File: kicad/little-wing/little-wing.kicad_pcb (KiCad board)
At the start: 4 copper layers, 14 x 42.1 mm, 68 parts, among them J1 HRO_TYPE-C-31-M-14, J2 Battery, J3 rgb, J4 columns, J5 Conn_01x10, J6 rows, J7 sensor, Q1 AO3401A, Q2 2N7002, SW1 Battery, SW2 Reset, U1 nRF52840_CKAA, U2 nPM1100-CAAx, X1 32MHz, X2 32.768kHz

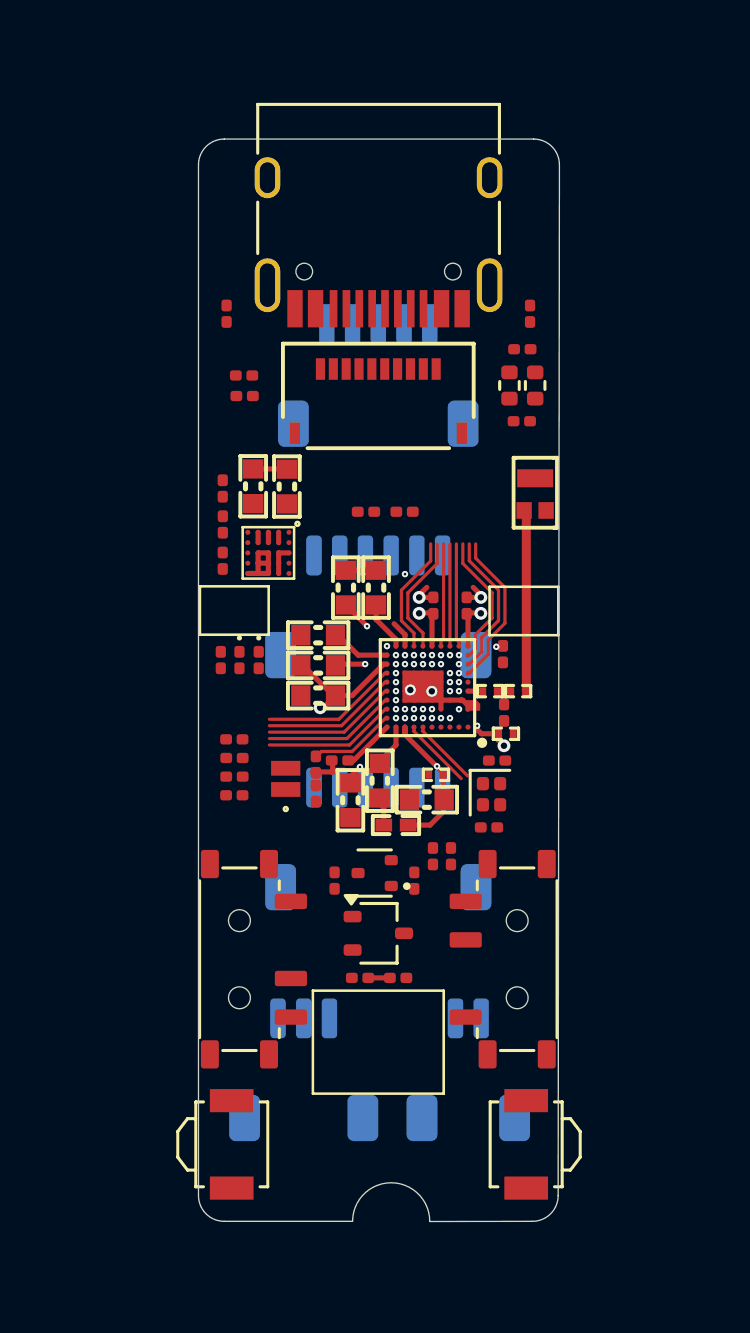
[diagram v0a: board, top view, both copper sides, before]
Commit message: Loosely attaching pins to prefiery
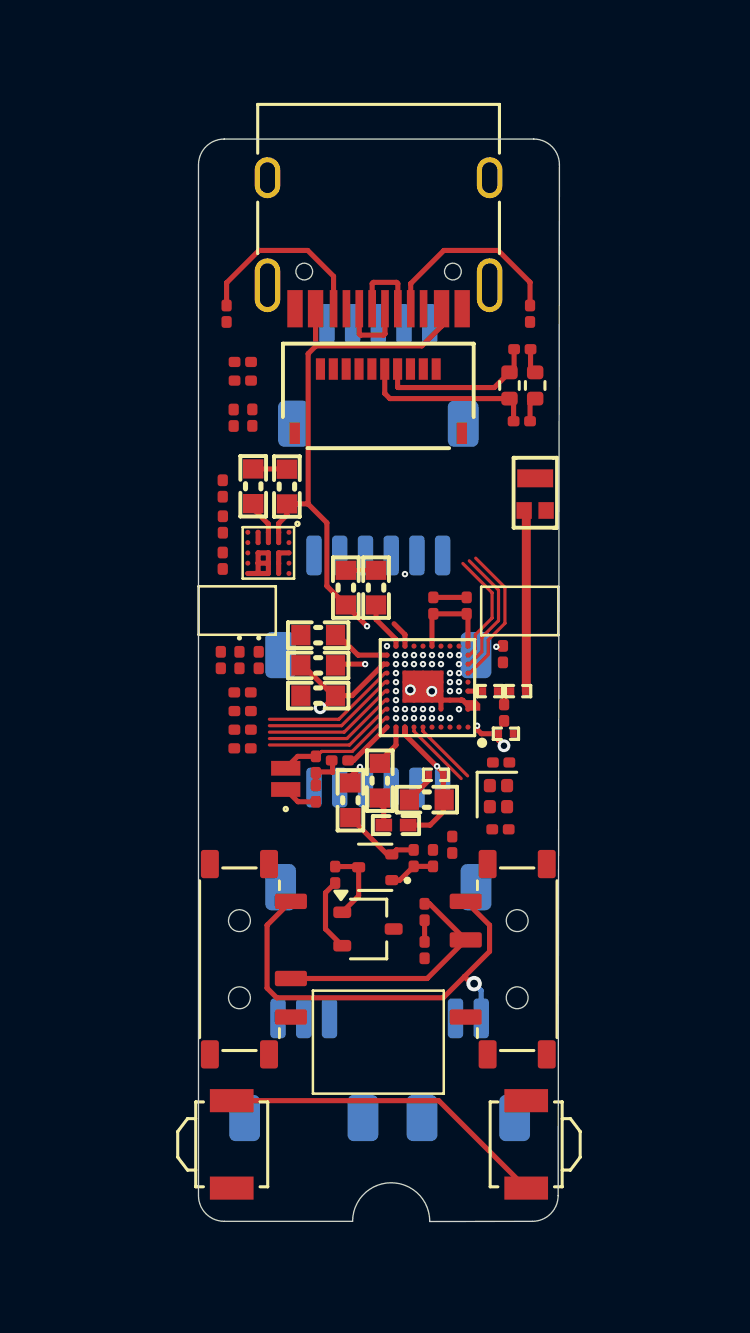
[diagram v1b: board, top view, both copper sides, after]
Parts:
- moved R32 6.96 mm to (145.1, 68.4), turned to -90 degrees
- moved R33 6.31 mm to (144.4, 68.4), turned to -90 degrees
- moved R_DIV1 3.59 mm to (151.8, 87.7), turned to -90 degrees
- moved R11 1.85 mm to (144.7, 79.1)
- moved R14 1.85 mm to (144.7, 79.8)
- moved R15 1.85 mm to (144.7, 80.6)
- moved R16 1.85 mm to (144.7, 81.3)
- moved R_DIV2 1.49 mm to (151.8, 89.1), turned to -90 degrees
- moved R18 0.88 mm to (151.4, 85.6)
- moved R39 0.60 mm to (144.7, 67.0)
- moved C37 0.53 mm to (144.7, 66.3)
- moved C2 0.45 mm to (154.8, 84.5)
- moved R8 0.45 mm to (152.9, 85.0)
- moved Q1 0.44 mm to (149.6, 88.3)
- moved X1 0.28 mm to (154.7, 83.2)
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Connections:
- J7 pad 1: GND -> VDD
- J7 pad 6: VDD -> GND
- U1 pad A5: unconnected-(U1-P0.03/AIN1-PadA5) -> VSENSE
- U1 pad A6: unconnected-(U1-P0.28/AIN4-PadA6) -> RGB DATA
- U1 pad A7: unconnected-(U1-P0.30/AIN6-PadA7) -> RGB ON
- U1 pad C10: unconnected-(U1-P0.04/AIN2-PadC10) -> Sensor IRQ
- U1 pad C8: VSENSE -> unconnected-(U1-P0.31/AIN7-PadC8)
- U1 pad D10: unconnected-(U1-P0.05/AIN3-PadD10) -> Sensor CLK
- U1 pad E10: unconnected-(U1-P0.08-PadE10) -> Sensor SDIO
- U1 pad F10: unconnected-(U1-P1.09-PadF10) -> Sensor CS
- U1 pad G1: unconnected-(U1-P1.07-PadG1) -> LCD CS
- U1 pad H1: unconnected-(U1-P1.04-PadH1) -> LCD DATA
- U1 pad J1: unconnected-(U1-P1.01-PadJ1) -> LCD CLK
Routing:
- net VBUS: track 3.49 -> 25.1 mm
- net Net-(J2-Pin_1): track 0.00 -> 17.6 mm, vias 0 -> 1
- net VBAT: track 0.70 -> 10.3 mm
- net RST: track 4.69 -> 12.9 mm
- net Net-(J1-CC1): track 0.00 -> 7.57 mm
- net Net-(J1-CC2): track 0.00 -> 7.24 mm
- net unconnected-(U1-P0.31/AIN7-PadC8): track 0.00 -> 7.05 mm, vias 0 -> 2
- net VSENSE: track 7.89 -> 0.84 mm, vias 2 -> 0
- net VDDA: track 0.00 -> 6.83 mm
- net VDD: track 15.4 -> 21.8 mm, vias 8 -> 6
- net unconnected-(U1-P1.07-PadG1): track 6.13 -> 0.00 mm
- net unconnected-(U1-P1.04-PadH1): track 5.67 -> 0.00 mm
- net LCD CS: track 0.00 -> 5.57 mm
- net unconnected-(U1-P1.09-PadF10): track 5.27 -> 0.00 mm
- net Sensor CS: track 0.00 -> 5.27 mm
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
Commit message: More routing
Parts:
- moved R11 0.12 mm to (144.8, 79.1)
- moved R15 0.12 mm to (144.8, 80.5)
- moved R16 0.12 mm to (144.8, 81.3)
- moved R14 0.12 mm to (144.8, 79.8)
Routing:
- net Net-(J3-Pin_2): track 0.00 -> 10.3 mm, vias 0 -> 1
- net Net-(J7-Pin_2): track 0.00 -> 9.98 mm, vias 0 -> 1
- net VSENSE: track 0.84 -> 10.7 mm
- net LCD CLK: track 4.46 -> 14.2 mm
- net LCD DATA: track 5.02 -> 14.6 mm
- net LCD CS: track 5.57 -> 15.0 mm
- net Net-(J7-Pin_3): track 0.00 -> 8.70 mm, vias 0 -> 1
- net Net-(J7-Pin_4): track 0.00 -> 7.38 mm, vias 0 -> 1
- net Net-(J7-Pin_5): track 0.00 -> 6.05 mm, vias 0 -> 1
- net unconnected-(U1-P1.05-PadG2): track 5.88 -> 0.00 mm
- net unconnected-(U1-P0.07-PadF9): track 5.75 -> 0.00 mm
- net unconnected-(U1-P0.06-PadE9): track 5.71 -> 0.00 mm
- net unconnected-(U1-P1.08-PadG9): track 5.79 -> 0.11 mm
- net unconnected-(U1-P0.27-PadD9): track 5.67 -> 0.00 mm
- net unconnected-(U1-P0.26-PadC9): track 5.63 -> 0.00 mm
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
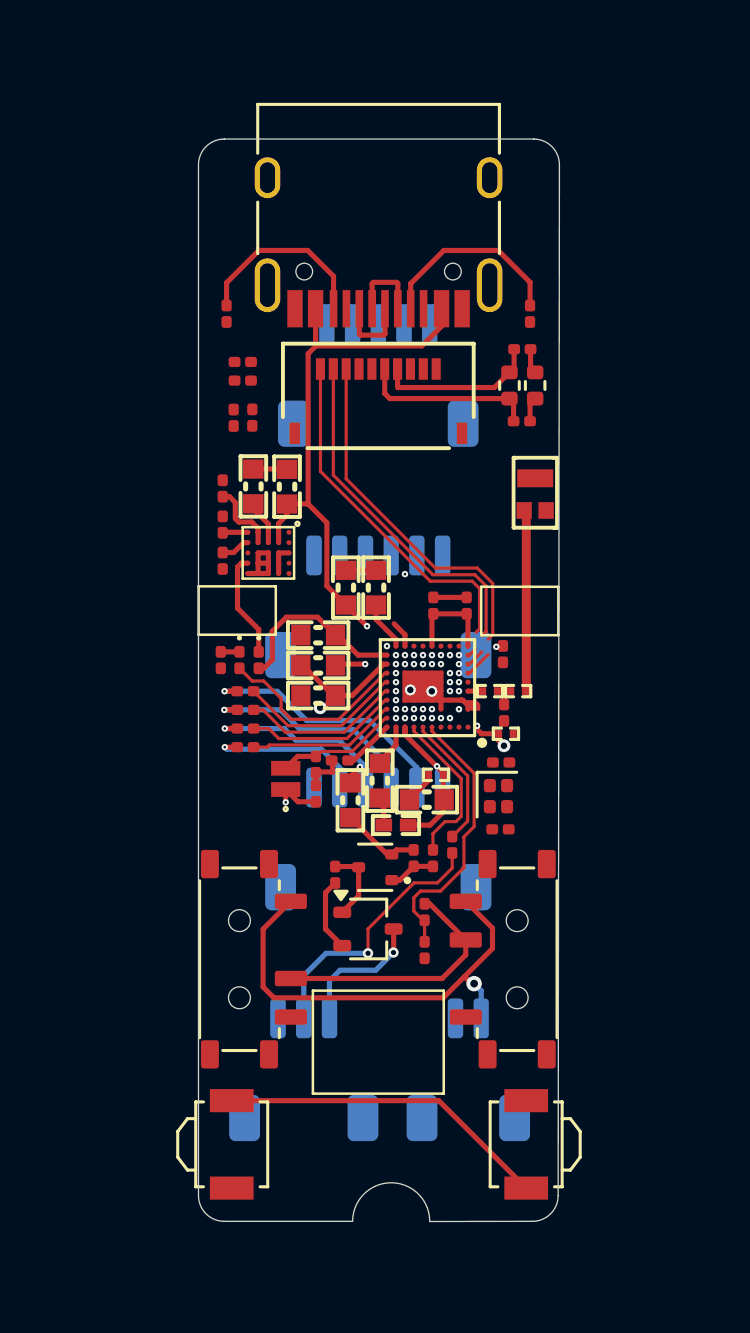
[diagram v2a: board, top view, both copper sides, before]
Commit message: Connecting most of the other components
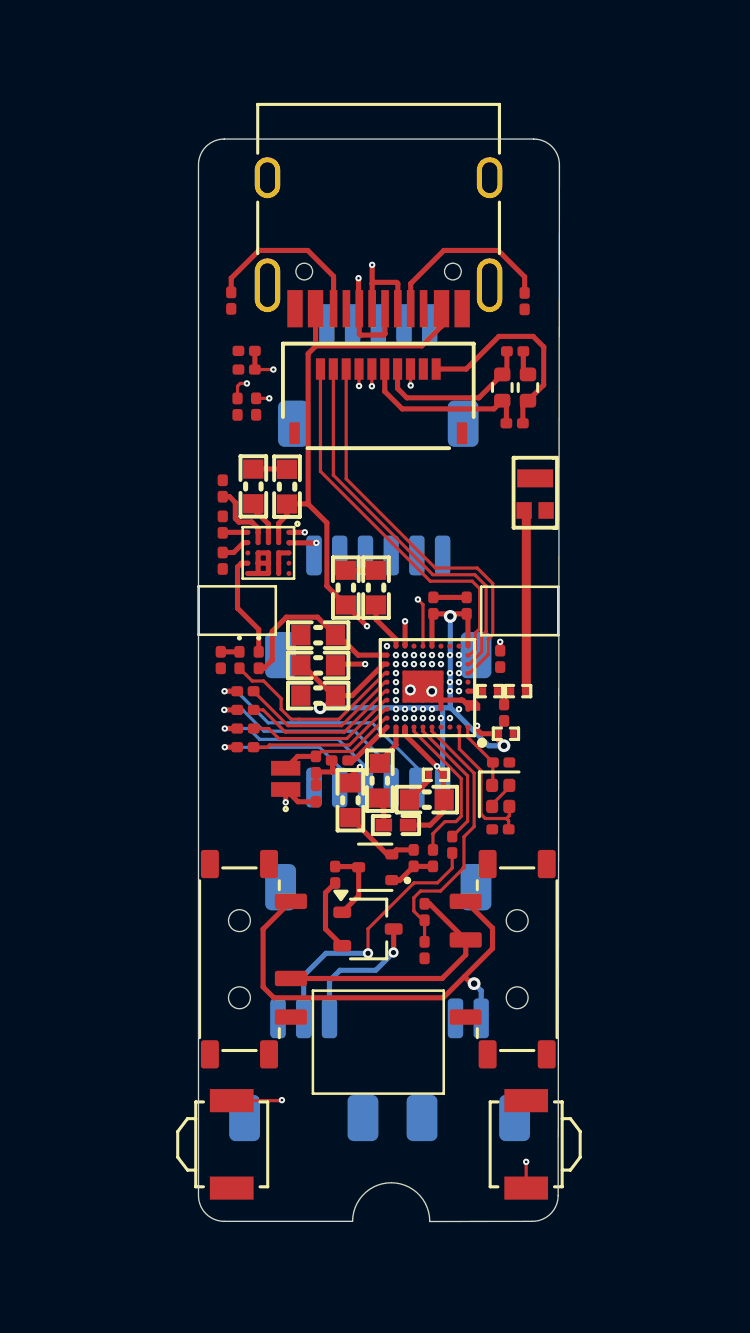
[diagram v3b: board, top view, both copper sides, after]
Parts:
- moved R22 0.54 mm to (144.3, 63.9)
- moved R21 0.53 mm to (155.7, 63.9)
- moved C37 0.46 mm to (144.9, 65.8)
- moved R39 0.46 mm to (144.9, 66.6)
- moved R32 0.46 mm to (145.2, 68.0)
- moved R33 0.46 mm to (144.5, 68.0)
- moved C30 0.29 mm to (155.3, 68.7)
- moved C38 0.29 mm to (155.3, 65.9)
- moved FB1 0.29 mm to (154.8, 67.3)
- moved FB2 0.29 mm to (155.8, 67.3)
- moved C9 0.21 mm to (154.7, 77.8)
- moved X1 0.09 mm to (154.8, 83.2)
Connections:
- X1 pad 2: unconnected-(X1-GND-Pad2) -> GND
- X1 pad 4: unconnected-(X1-GND-Pad4) -> GND
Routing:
- net RST: track 12.9 -> 37.5 mm, vias 0 -> 3
- net D+: track 4.04 -> 26.0 mm, vias 0 -> 3
- net D-: track 6.14 -> 26.1 mm, vias 2 -> 3
- net VDD: track 21.8 -> 37.3 mm, vias 6 -> 7
- net GNDA: track 0.96 -> 8.18 mm
- net EXTMODE: track 0.00 -> 6.86 mm, vias 0 -> 2
- net Net-(J5-Pin_5): track 0.00 -> 6.23 mm, vias 0 -> 2
- net EXTCOMIN: track 0.00 -> 5.95 mm, vias 0 -> 2
- net Net-(U1-XC2): track 0.00 -> 5.77 mm
- net unconnected-(U1-P1.10-PadB4): track 5.38 -> 0.00 mm
- net unconnected-(U1-P1.14-PadB5): track 5.34 -> 0.00 mm
- net unconnected-(U1-P0.02/AIN0-PadB6): track 5.30 -> 0.00 mm
- net Net-(U1-XC1): track 0.00 -> 2.69 mm
- net GND: track 19.5 -> 20.6 mm
- net LCD CLK: track 14.2 -> 14.9 mm
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
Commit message: Connecting remaining power lines
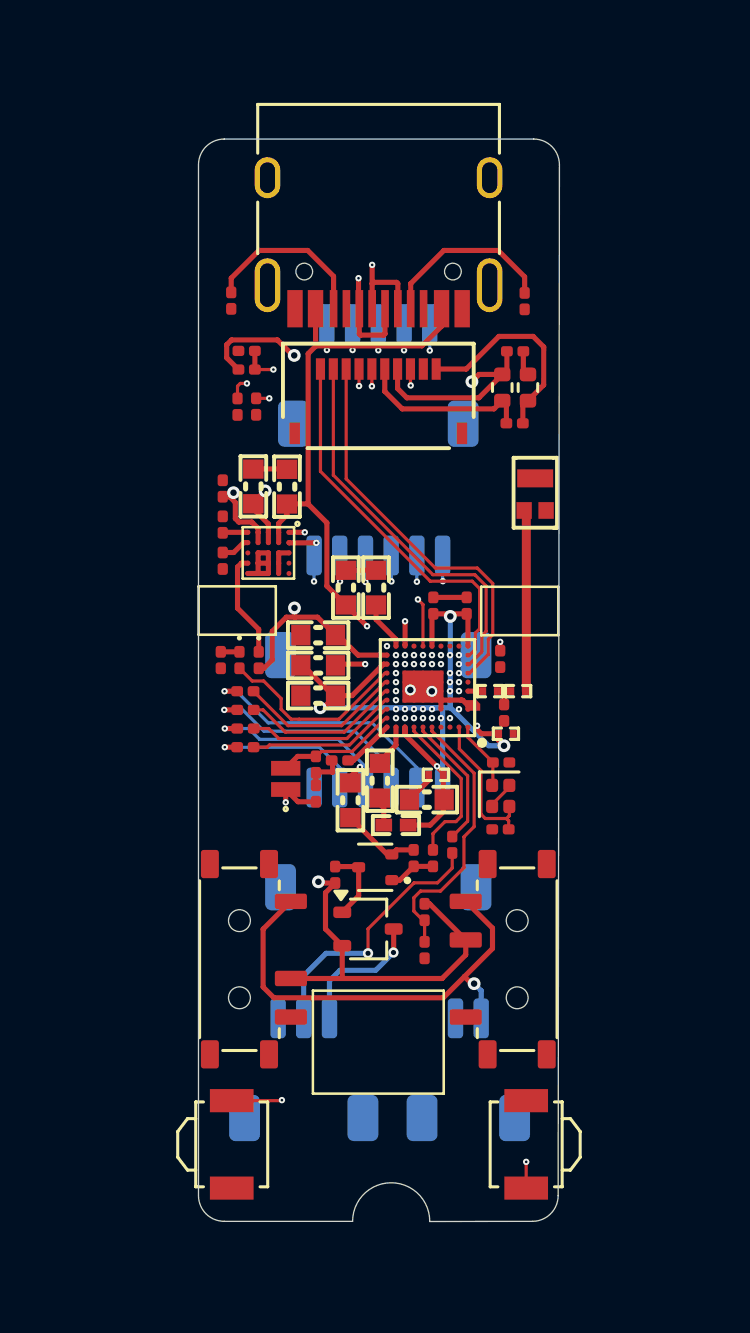
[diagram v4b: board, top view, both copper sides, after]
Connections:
- Q1 pad 2: VSYS -> VBAT
- R10 pad 1: VSYS -> VBAT
- U1 pad C6: unconnected-(U1-P1.15-PadC6) -> Col 5
- U1 pad C7: unconnected-(U1-P0.29/AIN5-PadC7) -> Row 4
- U1 pad C8: unconnected-(U1-P0.31/AIN7-PadC8) -> Col 4
- U1 pad E3: unconnected-(U1-P1.06-PadE3) -> Col 1
- U1 pad F3: unconnected-(U1-P1.03-PadF3) -> Col 0
- U1 pad G3: unconnected-(U1-P1.02-PadG3) -> Col 2
- U1 pad H4: unconnected-(U1-P0.24-PadH4) -> Row 0
- U1 pad H5: unconnected-(U1-P0.23-PadH5) -> Row 1
- U1 pad H6: unconnected-(U1-P0.16-PadH6) -> Col 3
- U1 pad H7: unconnected-(U1-P0.13-PadH7) -> Row 3
- U1 pad H8: unconnected-(U1-P0.11-PadH8) -> Row 2
- X1 pad 2: GND -> unconnected-(X1-GND-Pad2)
- X1 pad 4: GND -> unconnected-(X1-GND-Pad4)
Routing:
- net VDD: track 37.3 -> 59.5 mm, vias 7 -> 9
- net VBAT: track 13.0 -> 34.4 mm, vias 0 -> 2
- net Row 4: track 0.00 -> 17.3 mm, vias 0 -> 3
- net Row 3: track 0.00 -> 15.8 mm, vias 0 -> 3
- net Row 1: track 0.00 -> 15.3 mm, vias 0 -> 3
- net Row 0: track 0.00 -> 15.3 mm, vias 0 -> 3
- net Row 2: track 0.00 -> 14.7 mm, vias 0 -> 3
- net unconnected-(U1-P1.03-PadF3): track 13.4 -> 0.00 mm, vias 2 -> 0
- net unconnected-(U1-P1.06-PadE3): track 12.6 -> 0.00 mm, vias 2 -> 0
- net unconnected-(U1-P1.02-PadG3): track 11.0 -> 0.00 mm, vias 2 -> 0
- net Col 0: track 0.00 -> 10.2 mm, vias 0 -> 3
- net Col 5: track 0.00 -> 9.94 mm, vias 0 -> 3
- net unconnected-(U1-P0.24-PadH4): track 9.56 -> 0.00 mm, vias 2 -> 0
- net unconnected-(U1-P0.23-PadH5): track 9.47 -> 0.00 mm, vias 2 -> 0
- net unconnected-(U1-P0.16-PadH6): track 8.49 -> 0.00 mm, vias 2 -> 0
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
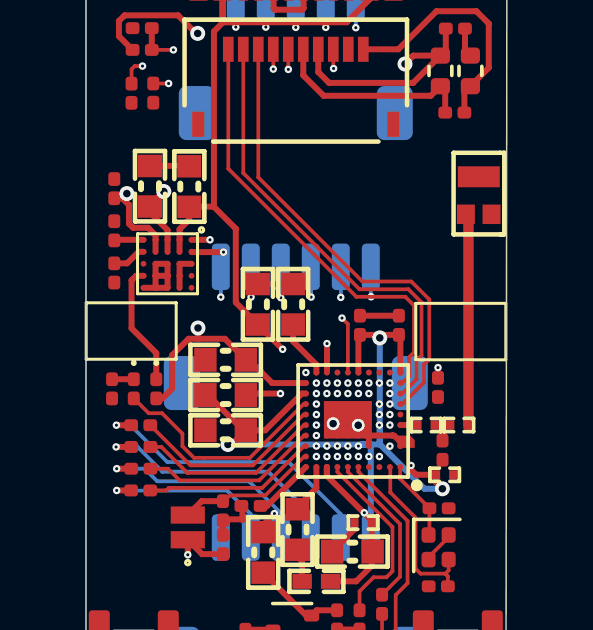
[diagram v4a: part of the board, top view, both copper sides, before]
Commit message: Adding the J-tag connector for the programmer
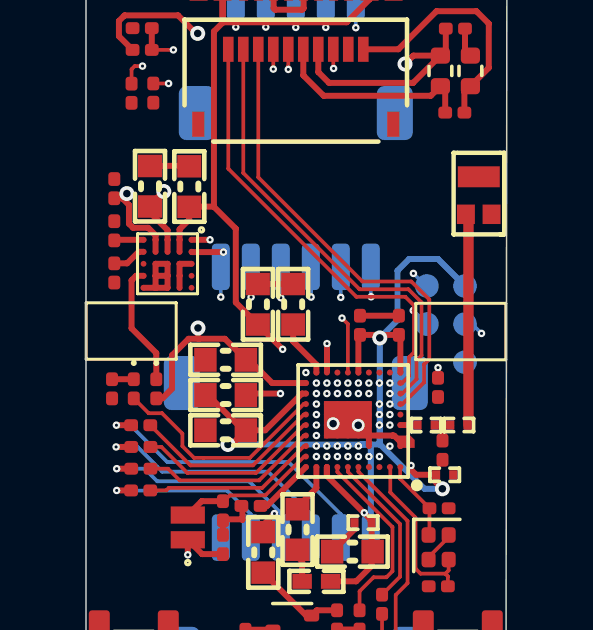
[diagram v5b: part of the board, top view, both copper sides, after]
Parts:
- added J8: Conn_ARM_SWD_TagConnect_TC2030-NL, Connector:Tag-Connect_TC2030-IDC-NL_2x03_P1.27mm_Vertical, B.Cu at (155.0, 75.7)
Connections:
- U1 pad H2: unconnected-(U1-SWDCLK-PadH2) -> SWCLK
- U1 pad J2: unconnected-(U1-SWDIO-PadJ2) -> SWDIO
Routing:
- net VDD: track 59.5 -> 64.8 mm
- net unconnected-(U1-SWDCLK-PadH2): track 4.89 -> 0.00 mm, vias 1 -> 0
- net SWDIO: track 0.00 -> 4.60 mm, vias 0 -> 2
- net unconnected-(U1-SWDIO-PadJ2): track 4.39 -> 0.00 mm, vias 1 -> 0
- net SWCLK: track 0.00 -> 3.79 mm, vias 0 -> 2
- net RST: track 37.5 -> 40.5 mm, vias 3 -> 4
